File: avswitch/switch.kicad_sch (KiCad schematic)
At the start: 125 parts, among them J501 Conn_01x06, J502 Conn_01x06, J503 Conn_01x06, J504 MUX_IN, J505 MUX_OUT, U501 RS8754, U502 RS8754, U503 RS8754, U504 RS8754, U505 RS8754, U506 RS8754, U507 74HC4052D, U508 74HC4052D, U509 74HC4052D

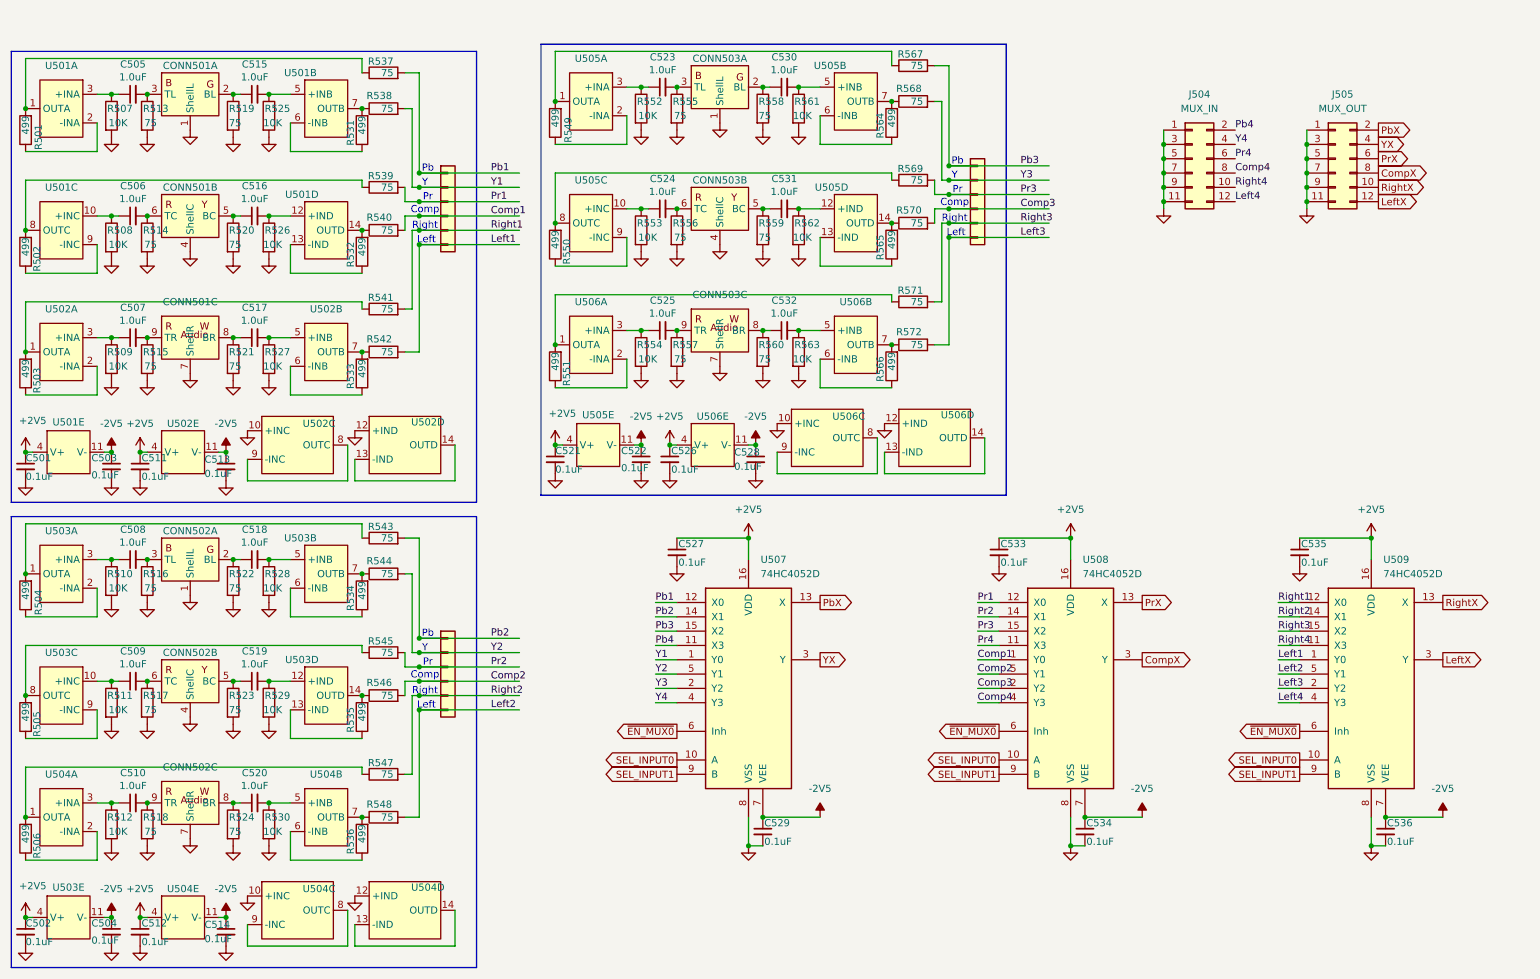
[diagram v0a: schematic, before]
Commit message: Recalculate for ceramic cap dc bias
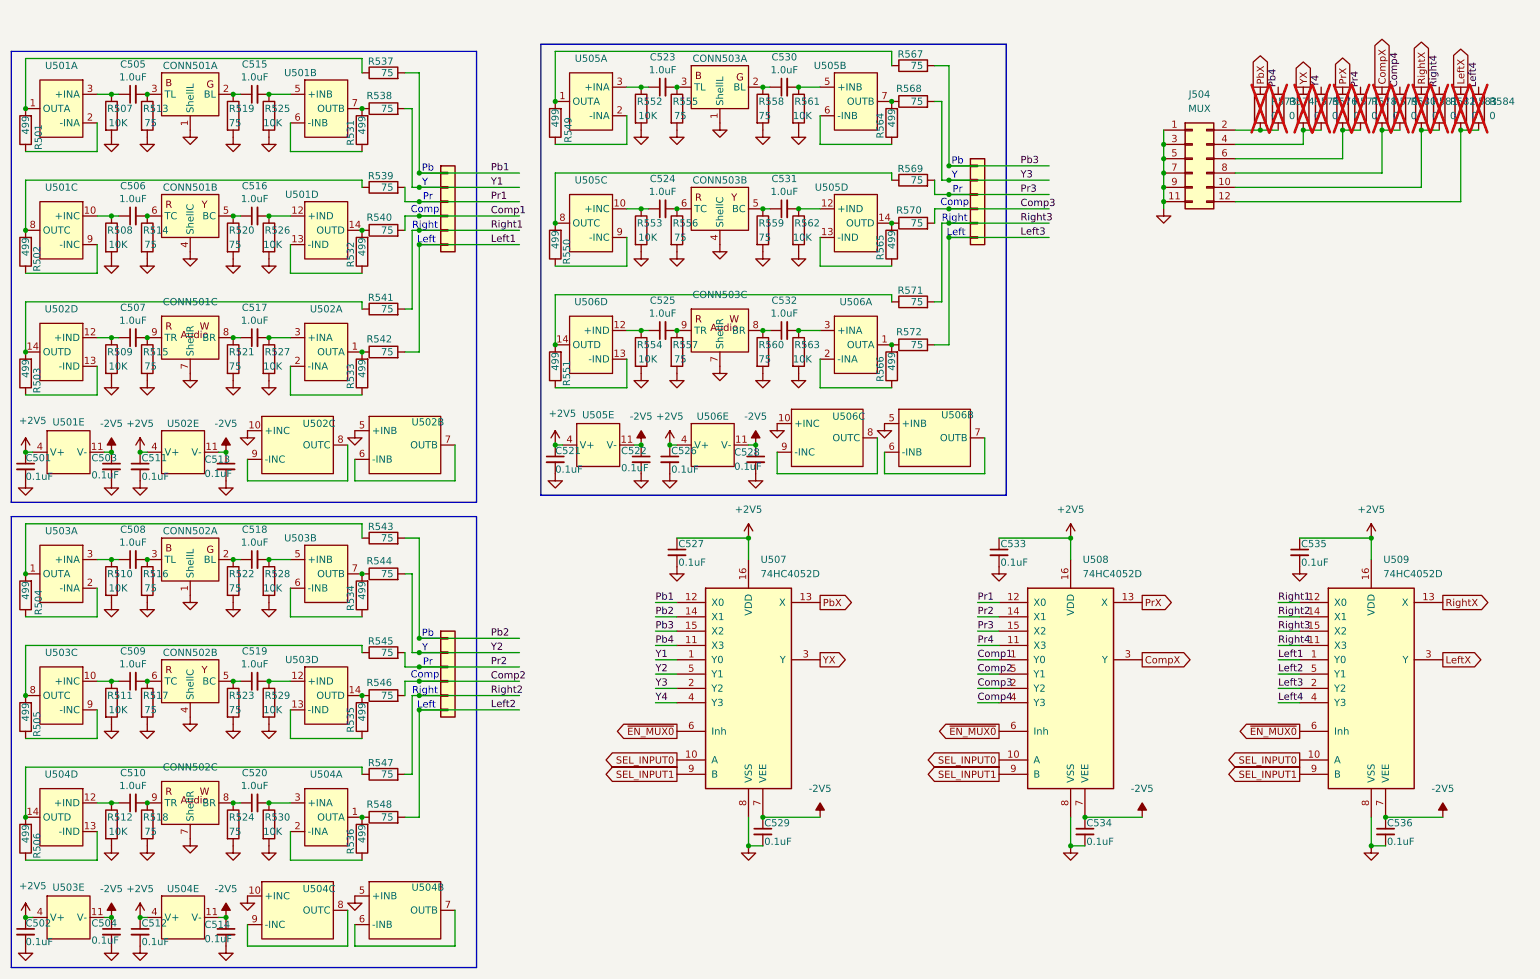
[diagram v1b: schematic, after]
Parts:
- removed J505: MUX_OUT, Connector_IDC:IDC-Header_2x06_P2.54mm_Horizontal, symbol Connector_Generic:Conn_02x06_Odd_Even
- added R573, R574, R575, R576, R577, R578, R579, R580, R581, R582, R583, R584: 0, Resistor_SMD:R_0805_2012Metric, symbol Device:R
- J504: value MUX_IN -> MUX; footprint Connector_IDC:IDC-Header_2x06_P2.54mm_Horizontal -> avswitch:amphenol-HLW12R-2C7LF
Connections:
- net Comp4: now also R580.2; no longer J504.8 (Pin_8)
- net CompX: now also R579.2
- net GND: now also U502.5 (+INB), U504.5 (+INB), U506.5 (+INB); no longer U502.12 (+IND), U504.12 (+IND), U506.12 (+IND)
- net Left4: now also R584.2; no longer J504.12 (Pin_12)
- net LeftX: now also R583.2
- net Pb4: now also R574.2; no longer J504.2 (Pin_2)
- net PbX: now also R573.2
- net Pr4: now also R578.2; no longer J504.6 (Pin_6)
- net PrX: now also R577.2
- net Right4: now also R582.2; no longer J504.10 (Pin_10)
- net RightX: now also R581.2
- net Y4: now also R576.2; no longer J504.4 (Pin_4)
- net YX: now also R575.2
- net at C517.2, R527.1: now also U502.3 (+INA); no longer U502.5 (+INB)
- net at R533.1: now also U502.2 (-INA); no longer U502.6 (-INB)
- net at R533.2, R542.1: now also U502.1 (OUTA); no longer U502.7 (OUTB)
- net at C520.2, R530.1: now also U504.3 (+INA); no longer U504.5 (+INB)
- net at R536.1: now also U504.2 (-INA); no longer U504.6 (-INB)
- net at R536.2, R548.1: now also U504.1 (OUTA); no longer U504.7 (OUTB)
- net at R506.1: now also U504.13 (-IND); no longer U504.2 (-INA)
- net at R506.2, R547.1: now also U504.14 (OUTD); no longer U504.1 (OUTA)
- net at R503.2, R541.1: now also U502.14 (OUTD); no longer U502.1 (OUTA)
- net at R503.1: now also U502.13 (-IND); no longer U502.2 (-INA)
- net at C507.1, R509.1: now also U502.12 (+IND); no longer U502.3 (+INA)
- net at C510.1, R512.1: now also U504.12 (+IND); no longer U504.3 (+INA)
- net at R551.2, R571.1: now also U506.14 (OUTD); no longer U506.1 (OUTA)
- net at C525.1, R554.1: now also U506.12 (+IND); no longer U506.3 (+INA)
- net at C532.2, R563.1: now also U506.3 (+INA); no longer U506.5 (+INB)
- net at R566.2, R572.1: now also U506.1 (OUTA); no longer U506.7 (OUTB)
- net at R566.1: now also U506.2 (-INA); no longer U506.6 (-INB)
- net at R551.1: now also U506.13 (-IND); no longer U506.2 (-INA)
- new net: U502.6 (-INB), U502.7 (OUTB)
- new net: J504.10 (Pin_10), R581.1, R582.1
- new net: J504.12 (Pin_12), R583.1, R584.1
- new net: J504.8 (Pin_8), R579.1, R580.1
- new net: J504.6 (Pin_6), R577.1, R578.1
- new net: J504.2 (Pin_2), R573.1, R574.1
- new net: J504.4 (Pin_4), R575.1, R576.1
- new net: U504.6 (-INB), U504.7 (OUTB)
- new net: U506.6 (-INB), U506.7 (OUTB)

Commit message: PCB Layout nearing completion
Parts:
- added D501, D502, D503, D504, D505, D506, D507, D508, D509, D510, D511, D512, D513, D514, D515, D516, D517, D518: D_TVS_Filled, Diode_SMD:D_SOD-323, symbol Device:D_TVS_Filled
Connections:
- net Comp1: now also U508.4 (Y3); no longer U508.1 (Y0)
- net Comp2: now also U508.2 (Y2); no longer U508.5 (Y1)
- net Comp3: now also U508.1 (Y0); no longer U508.2 (Y2)
- net Comp4: now also U508.5 (Y1); no longer U508.4 (Y3)
- net GND: now also D501.1 (A1), D502.1 (A1), D503.1 (A1), D504.1 (A1), D505.1 (A1), D506.1 (A1), D507.1 (A1), D508.1 (A1), D509.1 (A1), D510.1 (A1), D511.1 (A1), D512.1 (A1), D513.1 (A1), D514.1 (A1), D515.1 (A1), D516.1 (A1), D517.1 (A1), D518.1 (A1)
- net Left1: now also U509.4 (Y3); no longer U509.1 (Y0)
- net Left2: now also U509.2 (Y2); no longer U509.5 (Y1)
- net Left3: now also U509.1 (Y0); no longer U509.2 (Y2)
- net Left4: now also U509.5 (Y1); no longer U509.4 (Y3)
- net Pb1: now also U507.15 (X2); no longer U507.12 (X0)
- net Pb3: now also U507.12 (X0); no longer U507.15 (X2)
- net Pr1: now also U508.15 (X2); no longer U508.12 (X0)
- net Pr3: now also U508.12 (X0); no longer U508.15 (X2)
- net Y1: now also U507.4 (Y3); no longer U507.1 (Y0)
- net Y2: now also U507.2 (Y2); no longer U507.5 (Y1)
- net Y3: now also U507.1 (Y0); no longer U507.2 (Y2)
- net Y4: now also U507.5 (Y1); no longer U507.4 (Y3)
- net RCA_Y_2: now reaches C518.1, CONN502.2 (BL), R522.1
- net RCA_Y_2: now also D508.2 (A2)
- net RCA_Pb_2: now reaches C508.2, CONN502.3 (TL), R516.1
- net RCA_Pb_2: now also D507.2 (A2)
- net RCA_Left_1: now reaches C517.1, CONN501.8 (BR), R521.1
- net RCA_Left_1: now also D506.2 (A2)
- net RCA_Comp_1: now reaches C516.1, CONN501.5 (BC), R520.1
- net RCA_Comp_1: now also D504.2 (A2)
- net RCA_Pr_1: now reaches C506.2, CONN501.6 (TC), R514.1
- net RCA_Pr_1: now also D503.2 (A2)
- net RCA_Pr_3: now reaches C524.2, CONN503.6 (TC), R556.1
- net RCA_Pr_3: now also D515.2 (A2)
- net RCA_Y_1: now reaches C515.1, CONN501.2 (BL), R519.1
- net RCA_Y_1: now also D502.2 (A2)
- net RCA_Y_3: now reaches C530.1, CONN503.2 (BL), R558.1
- net RCA_Y_3: now also D514.2 (A2)
- net RCA_Left_2: now reaches C520.1, CONN502.8 (BR), R524.1
- net RCA_Left_2: now also D512.2 (A2)
- net RCA_Right_3: now reaches C525.2, CONN503.9 (TR), R557.1
- net RCA_Right_3: now also D517.2 (A2)
- net RCA_Left_3: now reaches C532.1, CONN503.8 (BR), R560.1
- net RCA_Left_3: now also D518.2 (A2)
- net RCA_Comp_3: now reaches C531.1, CONN503.5 (BC), R559.1
- net RCA_Comp_3: now also D516.2 (A2)
- net RCA_Right_2: now reaches C510.2, CONN502.9 (TR), R518.1
- net RCA_Right_2: now also D511.2 (A2)
- net RCA_Comp_2: now reaches C519.1, CONN502.5 (BC), R523.1
- net RCA_Comp_2: now also D510.2 (A2)
- net RCA_Pr_2: now reaches C509.2, CONN502.6 (TC), R517.1
- net RCA_Pr_2: now also D509.2 (A2)
- net RCA_Pb_3: now reaches C523.2, CONN503.3 (TL), R555.1
- net RCA_Pb_3: now also D513.2 (A2)
- net RCA_Pb_1: now reaches C505.2, CONN501.3 (TL), R513.1
- net RCA_Pb_1: now also D501.2 (A2)
- net RCA_Right_1: now reaches C507.2, CONN501.9 (TR), R515.1
- net RCA_Right_1: now also D505.2 (A2)

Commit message: V0.1 ordered from jlpcb
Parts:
- CONN501, CONN502, CONN503: value ~ -> SameSky RCJ-61562423
- R507, R508, R509, R510, R511, R512, R525, R526, R527, R528, R529, R530, R552, R553, R554, R561, R562, R563: value 10K -> 10k
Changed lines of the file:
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@@
 			)
 		)
-		(property "Value" "10K"
+		(property "Value" "10k"
 			(at 33.782 49.53 0)
 			(effects
@@
 			)
 		)
-		(property "Value" "~"
+		(property "Value" "SameSky RCJ-61562423"
 			(at 48.26 107.95 0)
 			(effects
@@
 			)
 		)
-		(property "Value" "~"
+		(property "Value" "SameSky RCJ-61562423"
 			(at 48.26 46.99 0)
 			(effects
@@
 			)
 		)
-		(property "Value" "10K"
+		(property "Value" "10k"
 			(at 61.214 71.12 0)
 			(effects
@@
 			)
 		)
-		(property "Value" "10K"
+		(property "Value" "10k"
 			(at 33.782 153.67 0)
 			(effects
@@
 			)
 		)
-		(property "Value" "10K"
+		(property "Value" "10k"
 			(at 61.214 110.49 0)
 			(effects
@@
 			)
 		)
-		(property "Value" "~"
+		(property "Value" "SameSky RCJ-61562423"
 			(at 142.24 67.31 0)
 			(effects
@@
 			)
 		)
-		(property "Value" "~"
+		(property "Value" "SameSky RCJ-61562423"
 			(at 142.24 45.72 0)
 			(effects
@@
 			)
 		)
-		(property "Value" "~"
+		(property "Value" "SameSky RCJ-61562423"
 			(at 48.26 129.54 0)
 			(effects
@@
 			)
 		)
-		(property "Value" "10K"
+		(property "Value" "10k"
 			(at 127.762 69.85 0)
 			(effects
@@
 			)
 		)
-		(property "Value" "10K"
+		(property "Value" "10k"
 			(at 33.782 71.12 0)
 			(effects
@@
 			)
 		)
-		(property "Value" "10K"
+		(property "Value" "10k"
 			(at 33.782 27.94 0)
 			(effects
@@
 			)
 		)
-		(property "Value" "10K"
+		(property "Value" "10k"
 			(at 33.782 110.49 0)
 			(effects
@@
 			)
 		)
-		(property "Value" "10K"
+		(property "Value" "10k"
 			(at 155.194 26.67 0)
 			(effects
@@
 			)
 		)
-		(property "Value" "10K"
+		(property "Value" "10k"
 			(at 33.782 132.08 0)
 			(effects
@@
 			)
 		)
-		(property "Value" "10K"
+		(property "Value" "10k"
 			(at 155.194 69.85 0)
 			(effects
@@
 			)
 		)
-		(property "Value" "10K"
+		(property "Value" "10k"
 			(at 155.194 48.26 0)
 			(effects
@@
 			)
 		)
-		(property "Value" "10K"
+		(property "Value" "10k"
 			(at 61.214 153.67 0)
 			(effects
@@
 			)
 		)
-		(property "Value" "~"
+		(property "Value" "SameSky RCJ-61562423"
 			(at 48.26 68.58 0)
 			(effects
@@
 			)
 		)
-		(property "Value" "10K"
+		(property "Value" "10k"
 			(at 61.214 49.53 0)
 			(effects
@@
 			)
 		)
-		(property "Value" "10K"
+		(property "Value" "10k"
 			(at 127.762 26.67 0)
 			(effects
@@
 			)
 		)
-		(property "Value" "10K"
+		(property "Value" "10k"
 			(at 61.214 132.08 0)
 			(effects
@@
 			)
 		)
-		(property "Value" "10K"
+		(property "Value" "10k"
 			(at 61.214 27.94 0)
 			(effects
@@
 			)
 		)
-		(property "Value" "~"
+		(property "Value" "SameSky RCJ-61562423"
 			(at 142.24 24.13 0)
 			(effects
@@
 			)
 		)
-		(property "Value" "10K"
+		(property "Value" "10k"
 			(at 127.762 48.26 0)
 			(effects
@@
 			)
 		)
-		(property "Value" "~"
+		(property "Value" "SameSky RCJ-61562423"
 			(at 48.26 25.4 0)
 			(effects
@@
 			)
 		)
-		(property "Value" "~"
+		(property "Value" "SameSky RCJ-61562423"
 			(at 48.26 151.13 0)
 			(effects
